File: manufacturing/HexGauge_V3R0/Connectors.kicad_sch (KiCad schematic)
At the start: 17 parts, among them J1 USB_B_Micro, J2 Conn_ARM_SWD_TC2030-NL, J3 Micro_SD_Card, J4 Conn_01x04_Pin, SW2 SW_Omron_B3FS, U4 USBLC6-4

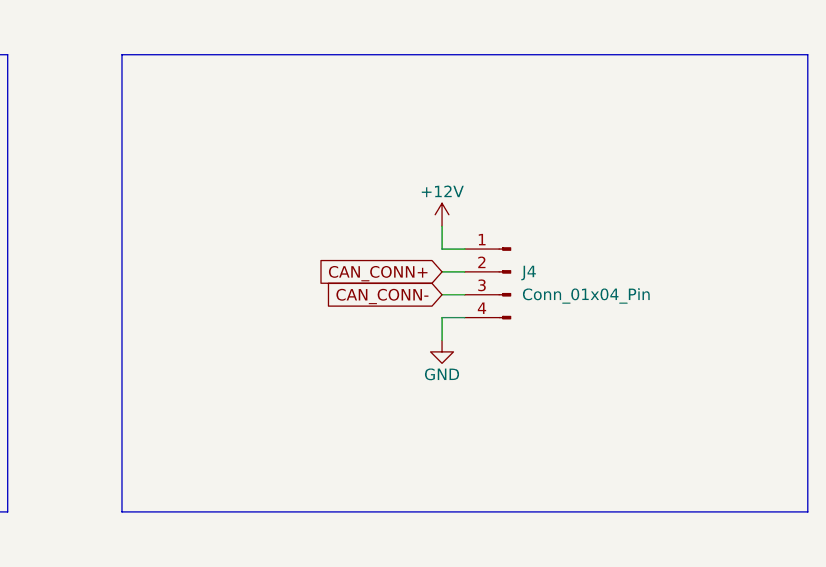
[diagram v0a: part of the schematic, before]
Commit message: Updated Board
Added Mounting Hole and 3D Packages
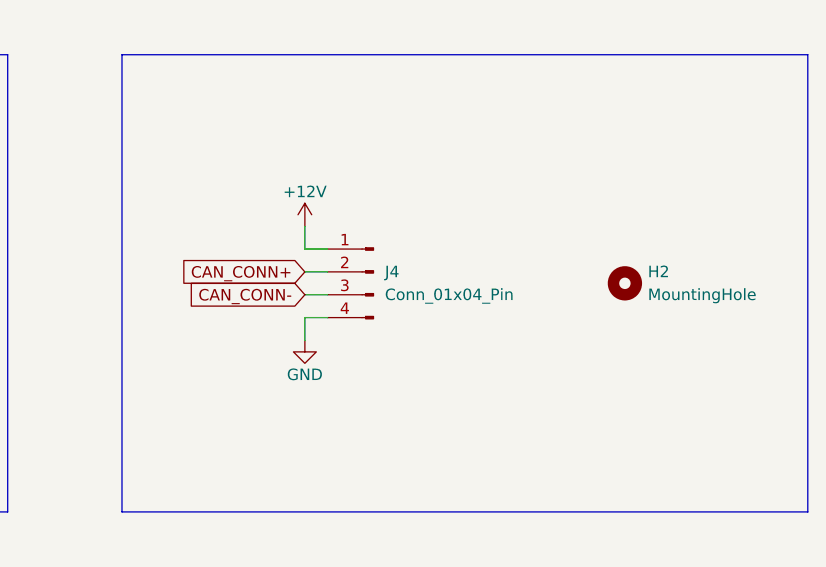
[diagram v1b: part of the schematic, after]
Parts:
- added H2: MountingHole, MountingHole:MountingHole_3.2mm_M3_Pad_Via, symbol Mechanical:MountingHole
- J1: LCSC Part # C319160 -> C397452
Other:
- moved on the sheet: J4
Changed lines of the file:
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@@
     (stroke (width 0) (type default))
   )
-  (wire (pts (xy 226.06 128.27) (xy 228.6 128.27))
+  (wire (pts (xy 210.82 128.27) (xy 213.36 128.27))
     (stroke (width 0) (type default))
   )
@@
     (stroke (width 0) (type default))
   )
-  (wire (pts (xy 226.06 125.73) (xy 228.6 125.73))
+  (wire (pts (xy 210.82 125.73) (xy 213.36 125.73))
     (stroke (width 0) (type default))
   )
@@
     (stroke (width 0) (type default))
   )
-  (wire (pts (xy 226.06 120.65) (xy 226.06 123.19))
+  (wire (pts (xy 210.82 120.65) (xy 210.82 123.19))
     (stroke (width 0) (type default))
   )
@@
     (stroke (width 0) (type default))
   )
-  (wire (pts (xy 226.06 123.19) (xy 228.6 123.19))
+  (wire (pts (xy 210.82 123.19) (xy 213.36 123.19))
     (stroke (width 0) (type default))
   )
@@
     (stroke (width 0) (type default))
   )
-  (wire (pts (xy 226.06 130.81) (xy 228.6 130.81))
+  (wire (pts (xy 210.82 130.81) (xy 213.36 130.81))
     (stroke (width 0) (type default))
   )
@@
     (stroke (width 0) (type default))
   )
-  (wire (pts (xy 226.06 130.81) (xy 226.06 133.35))
+  (wire (pts (xy 210.82 130.81) (xy 210.82 133.35))
     (stroke (width 0) (type default))
   )
@@
     )
   )
-  (global_label "CAN_CONN+" (shape input) (at 226.06 125.73 180) (fields_autoplaced)
-    (effects (font (size 1.27 1.27)) (justify right))
-    (property "Intersheetrefs" "${INTERSHEET_REFS}" (at 211.6636 125.73 0)
+  (global_label "CAN_CONN+" (shape input) (at 210.82 125.73 180) (fields_autoplaced)
+    (effects (font (size 1.27 1.27)) (justify right))
+    (property "Intersheetrefs" "${INTERSHEET_REFS}" (at 196.4236 125.73 0)
       (effects (font (size 1.27 1.27)) (justify right) hide)
     )
@@
     )
   )
-  (global_label "CAN_CONN-" (shape input) (at 226.06 128.27 180) (fields_autoplaced)
-    (effects (font (size 1.27 1.27)) (justify right))
-    (property "Intersheetrefs" "${INTERSHEET_REFS}" (at 211.6636 128.27 0)
+  (global_label "CAN_CONN-" (shape input) (at 210.82 128.27 180) (fields_autoplaced)
+    (effects (font (size 1.27 1.27)) (justify right))
+    (property "Intersheetrefs" "${INTERSHEET_REFS}" (at 196.4236 128.27 0)
       (effects (font (size 1.27 1.27)) (justify right) hide)
     )
@@
     )
   )
-  (symbol (lib_id "power:+12V") (at 226.06 120.65 0) (unit 1)
-    (in_bom yes) (on_board yes) (dnp no)
-    (property "Reference" "#PWR056" (at 226.06 124.46 0)
-      (effects (font (size 1.27 1.27)) hide)
-    )
-    (property "Value" "+12V" (at 226.06 116.84 0)
-      (effects (font (size 1.27 1.27)))
-    )
-    (property "Footprint" "" (at 226.06 120.65 0)
-      (effects (font (size 1.27 1.27)) hide)
-    )
-    (property "Datasheet" "" (at 226.06 120.65 0)
+  (symbol (lib_id "power:+12V") (at 210.82 120.65 0) (unit 1)
+    (in_bom yes) (on_board yes) (dnp no)
+    (property "Reference" "#PWR056" (at 210.82 124.46 0)
+      (effects (font (size 1.27 1.27)) hide)
+    )
+    (property "Value" "+12V" (at 210.82 116.84 0)
+      (effects (font (size 1.27 1.27)))
+    )
+    (property "Footprint" "" (at 210.82 120.65 0)
+      (effects (font (size 1.27 1.27)) hide)
+    )
+    (property "Datasheet" "" (at 210.82 120.65 0)
       (effects (font (size 1.27 1.27)) hide)
     )
@@
       (effects (font (size 1.27 1.27)) hide)
     )
-    (property "LCSC Part #" "C319160" (at 81.28 58.42 0)
+    (property "LCSC Part #" "C397452" (at 81.28 58.42 0)
       (effects (font (size 1.27 1.27)) hide)
     )
@@
     )
   )
+  (symbol (lib_id "Mechanical:MountingHole") (at 246.38 127 0) (unit 1)
+    (in_bom yes) (on_board yes) (dnp no) (fields_autoplaced)
+    (property "Reference" "H2" (at 248.92 125.73 0)
+      (effects (font (size 1.27 1.27)) (justify left))
+    )
+    (property "Value" "MountingHole" (at 248.92 128.27 0)
+      (effects (font (size 1.27 1.27)) (justify left))
+    )
+    (property "Footprint" "MountingHole:MountingHole_3.2mm_M3_Pad_Via" (at 246.38 127 0)
+      (effects (font (size 1.27 1.27)) hide)
+    )
+    (property "Datasheet" "~" (at 246.38 127 0)
+      (effects (font (size 1.27 1.27)) hide)
+    )
+    (instances
+      (project "STM32F4_HexGauge_V3"
+        (path "/1671c3d2-535f-4cd5-a65b-02e5c9ad18e5/6132b015-8d81-4c9d-ab7f-afd3c7f45a00"
+          (reference "H2") (unit 1)
+        )
+      )
+    )
+  )
   (symbol (lib_id "power:GND") (at 152.4 76.2 0) (unit 1)
     (in_bom yes) (on_board yes) (dnp no)
@@
     )
   )
-  (symbol (lib_id "Connector:Conn_01x04_Pin") (at 233.68 125.73 0) (mirror y) (unit 1)
+  (symbol (lib_id "Connector:Conn_01x04_Pin") (at 218.44 125.73 0) (mirror y) (unit 1)
     (in_bom yes) (on_board yes) (dnp no) (fields_autoplaced)
-    (property "Reference" "J4" (at 234.95 125.73 0)
+    (property "Reference" "J4" (at 219.71 125.73 0)
       (effects (font (size 1.27 1.27)) (justify right))
     )
-    (property "Value" "Conn_01x04_Pin" (at 234.95 128.27 0)
+    (property "Value" "Conn_01x04_Pin" (at 219.71 128.27 0)
       (effects (font (size 1.27 1.27)) (justify right))
     )
-    (property "Footprint" "Connector_Molex:Molex_Micro-Latch_53253-0470_1x04_P2.00mm_Vertical" (at 233.68 125.73 0)
-      (effects (font (size 1.27 1.27)) hide)
-    )
-    (property "Datasheet" "~" (at 233.68 125.73 0)
+    (property "Footprint" "Connector_Molex:Molex_Micro-Latch_53253-0470_1x04_P2.00mm_Vertical" (at 218.44 125.73 0)
+      (effects (font (size 1.27 1.27)) hide)
+    )
+    (property "Datasheet" "~" (at 218.44 125.73 0)
       (effects (font (size 1.27 1.27)) hide)
     )
@@
     )
   )
-  (symbol (lib_id "power:GND") (at 226.06 133.35 0) (unit 1)
-    (in_bom yes) (on_board yes) (dnp no)
-    (property "Reference" "#PWR057" (at 226.06 139.7 0)
-      (effects (font (size 1.27 1.27)) hide)
-    )
-    (property "Value" "GND" (at 226.06 137.16 0)
-      (effects (font (size 1.27 1.27)))
-    )
-    (property "Footprint" "" (at 226.06 133.35 0)
-      (effects (font (size 1.27 1.27)) hide)
-    )
-    (property "Datasheet" "" (at 226.06 133.35 0)
-      (effects (font (size 1.27 1.27)) hide)
-    )
+  (symbol (lib_id "power:GND") (at 210.82 133.35 0) (unit 1)
+    (in_bom yes) (on_board yes) (dnp no)
+    (property "Reference" "#PWR057" (at 210.82 139.7 0)
+      (effects (font (size 1.27 1.27)) hide)
+    )
+    (property "Value" "GND" (at 210.82 137.16 0)
+      (effects (font (size 1.27 1.27)))
+    )
+    (property "Footprint" "" (at 210.82 133.35 0)
+      (effects (font (size 1.27 1.27)) hide)
+    )
+    (property "Datasheet" "" (at 210.82 133.35 0)
+      (effects (font (size 1.27 1.27)) hide)
+    )

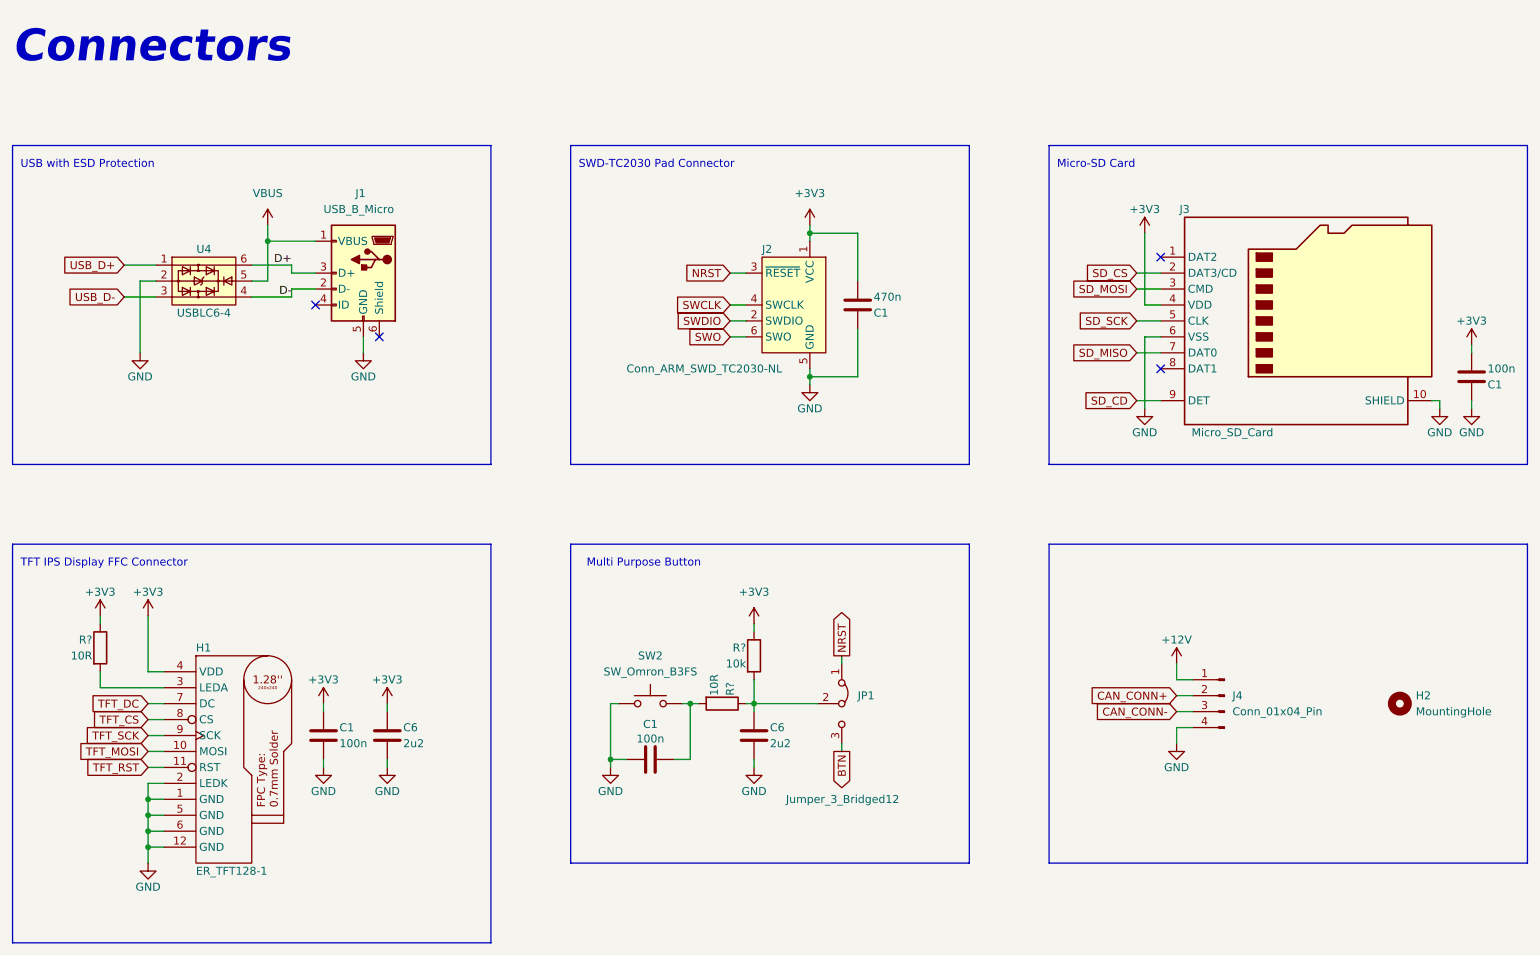
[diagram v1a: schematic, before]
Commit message: Updated Board and added Images
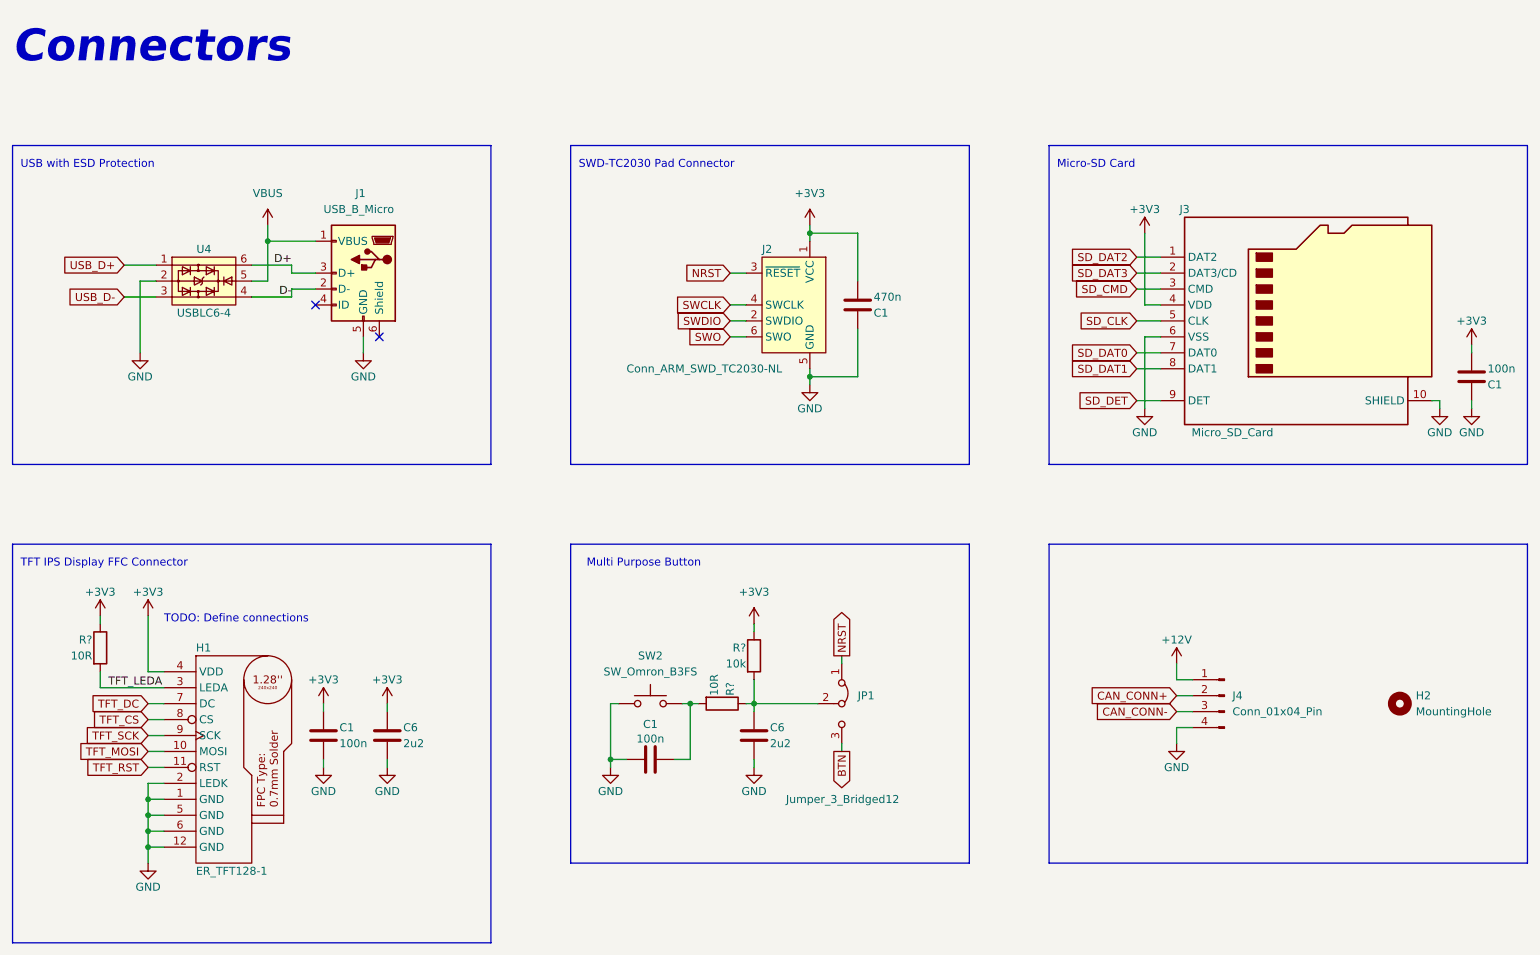
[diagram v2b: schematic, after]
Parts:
- C1: footprint Capacitor_SMD:C_0402_1005Metric -> Capacitor_SMD:C_0805_2012Metric_Pad1.18x1.45mm_HandSolder; LCSC Part # C1525 -> (none)
- C6: footprint Capacitor_SMD:C_0603_1608Metric -> Capacitor_SMD:C_0805_2012Metric_Pad1.18x1.45mm_HandSolder; LCSC Part # C23630 -> (none)
- R?: footprint Resistor_SMD:R_0402_1005Metric -> Resistor_SMD:R_0805_2012Metric_Pad1.20x1.40mm_HandSolder; LCSC Part # C25077 -> (none)
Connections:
- net TFT_LEDA: now reaches H1.3 (LEDA), R?.2
- net SD_DAT2: now reaches J3.1 (DAT2)
- net SD_DAT1: now reaches J3.8 (DAT1)
- net SD_CD renamed SD_DET
- net SD_CS renamed SD_DAT3
- net SD_MISO renamed SD_DAT0
- net SD_MOSI renamed SD_CMD
- net SD_SCK renamed SD_CLK
- no-connect marks 4 -> 2
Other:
- note added: "TODO: Define connections"
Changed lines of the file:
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@@
   (junction (at 120.65 135.89) (diameter 0) (color 0 0 0 0)
   )
-  (no_connect (at 208.28 73.66))
   (no_connect (at 73.66 63.5))
   (no_connect (at 83.82 68.58))
-  (no_connect (at 208.28 55.88))
   (wire (pts (xy 46.99 139.7) (xy 46.99 142.24))
     (stroke (width 0) (type default))
@@
     (stroke (width 0) (type default))
   )
+  (wire (pts (xy 204.47 55.88) (xy 208.28 55.88))
+    (stroke (width 0) (type default))
+  )
   (wire (pts (xy 210.82 120.65) (xy 210.82 123.19))
     (stroke (width 0) (type default))
@@
   )
   (wire (pts (xy 139.7 68.58) (xy 142.24 68.58))
+    (stroke (width 0) (type default))
+  )
+  (wire (pts (xy 204.47 73.66) (xy 208.28 73.66))
     (stroke (width 0) (type default))
   )
@@
     (effects (font (size 1.27 1.27)) (justify left bottom))
   )
+  (text "TODO: Define connections" (at 49.53 114.3 0)
+    (effects (font (size 1.27 1.27)) (justify left bottom))
+  )
   (text "Connectors" (at 25.4 25.4 0)
     (effects (font (size 5.08 5.08) (thickness 1.016) bold italic) (justify left bottom))
@@
     (effects (font (size 1.27 1.27)) (justify left bottom))
   )
+  (label "TFT_LEDA" (at 40.64 124.46 0) (fields_autoplaced)
+    (effects (font (size 1.27 1.27)) (justify left bottom))
+  )
   (label "D+" (at 69.85 57.15 180) (fields_autoplaced)
     (effects (font (size 1.27 1.27)) (justify right bottom))
@@
     )
   )
-  (global_label "SD_CD" (shape input) (at 204.47 78.74 180) (fields_autoplaced)
-    (effects (font (size 1.27 1.27)) (justify right))
-    (property "Intersheetrefs" "${INTERSHEET_REFS}" (at 195.5771 78.74 0)
-      (effects (font (size 1.27 1.27)) (justify right) hide)
-    )
-  )
-  (global_label "SD_CS" (shape input) (at 204.47 58.42 180) (fields_autoplaced)
-    (effects (font (size 1.27 1.27)) (justify right))
-    (property "Intersheetrefs" "${INTERSHEET_REFS}" (at 195.6376 58.42 0)
+  (global_label "SD_DET" (shape input) (at 204.47 78.74 180) (fields_autoplaced)
+    (effects (font (size 1.27 1.27)) (justify right))
+    (property "Intersheetrefs" "${INTERSHEET_REFS}" (at 194.7305 78.74 0)
+      (effects (font (size 1.27 1.27)) (justify right) hide)
+    )
+  )
+  (global_label "SD_DAT2" (shape input) (at 204.47 55.88 180) (fields_autoplaced)
+    (effects (font (size 1.27 1.27)) (justify right))
+    (property "Intersheetrefs" "${INTERSHEET_REFS}" (at 193.5814 55.88 0)
+      (effects (font (size 1.27 1.27)) (justify right) hide)
+    )
+  )
+  (global_label "SD_DAT3" (shape input) (at 204.47 58.42 180) (fields_autoplaced)
+    (effects (font (size 1.27 1.27)) (justify right))
+    (property "Intersheetrefs" "${INTERSHEET_REFS}" (at 193.5814 58.42 0)
       (effects (font (size 1.27 1.27)) (justify right) hide)
     )
@@
     )
   )
-  (global_label "SD_MOSI" (shape input) (at 204.47 60.96 180) (fields_autoplaced)
-    (effects (font (size 1.27 1.27)) (justify right))
-    (property "Intersheetrefs" "${INTERSHEET_REFS}" (at 193.5209 60.96 0)
+  (global_label "SD_CMD" (shape input) (at 204.47 60.96 180) (fields_autoplaced)
+    (effects (font (size 1.27 1.27)) (justify right))
+    (property "Intersheetrefs" "${INTERSHEET_REFS}" (at 194.1257 60.96 0)
       (effects (font (size 1.27 1.27)) (justify right) hide)
     )
@@
     )
   )
-  (global_label "SD_MISO" (shape input) (at 204.47 71.12 180) (fields_autoplaced)
-    (effects (font (size 1.27 1.27)) (justify right))
-    (property "Intersheetrefs" "${INTERSHEET_REFS}" (at 193.5209 71.12 0)
-      (effects (font (size 1.27 1.27)) (justify right) hide)
-    )
-  )
-  (global_label "SD_SCK" (shape input) (at 204.47 66.04 180) (fields_autoplaced)
-    (effects (font (size 1.27 1.27)) (justify right))
-    (property "Intersheetrefs" "${INTERSHEET_REFS}" (at 194.3676 66.04 0)
+  (global_label "SD_DAT0" (shape input) (at 204.47 71.12 180) (fields_autoplaced)
+    (effects (font (size 1.27 1.27)) (justify right))
+    (property "Intersheetrefs" "${INTERSHEET_REFS}" (at 193.5814 71.12 0)
+      (effects (font (size 1.27 1.27)) (justify right) hide)
+    )
+  )
+  (global_label "SD_CLK" (shape input) (at 204.47 66.04 180) (fields_autoplaced)
+    (effects (font (size 1.27 1.27)) (justify right))
+    (property "Intersheetrefs" "${INTERSHEET_REFS}" (at 194.549 66.04 0)
+      (effects (font (size 1.27 1.27)) (justify right) hide)
+    )
+  )
+  (global_label "SD_DAT1" (shape input) (at 204.47 73.66 180) (fields_autoplaced)
+    (effects (font (size 1.27 1.27)) (justify right))
+    (property "Intersheetrefs" "${INTERSHEET_REFS}" (at 193.5814 73.66 0)
       (effects (font (size 1.27 1.27)) (justify right) hide)
     )
@@
       (effects (font (size 1.27 1.27)) (justify left))
     )
-    (property "Footprint" "Capacitor_SMD:C_0402_1005Metric" (at 258.7752 78.74 0)
+    (property "Footprint" "Capacitor_SMD:C_0805_2012Metric_Pad1.18x1.45mm_HandSolder" (at 258.7752 78.74 0)
       (effects (font (size 1.27 1.27)) hide)
     )
@@
       (effects (font (size 1.27 1.27)) hide)
     )
-    (property "LCSC Part #" "C1525" (at 257.81 74.93 0)
+    (property "LCSC Part #" "" (at 257.81 74.93 0)
       (effects (font (size 1.27 1.27)) hide)
     )
@@
       (effects (font (size 1.27 1.27)) (justify left))
     )
-    (property "Footprint" "Capacitor_SMD:C_0603_1608Metric" (at 86.0552 135.89 0)
+    (property "Footprint" "Capacitor_SMD:C_0805_2012Metric_Pad1.18x1.45mm_HandSolder" (at 86.0552 135.89 0)
       (effects (font (size 1.27 1.27)) hide)
     )
@@
       (effects (font (size 1.27 1.27)) hide)
     )
-    (property "LCSC Part #" "C23630" (at 85.09 132.08 0)
+    (property "LCSC Part #" "" (at 85.09 132.08 0)
       (effects (font (size 1.27 1.27)) hide)
     )
@@
       (effects (font (size 1.27 1.27)) (justify right))
     )
-    (property "Footprint" "Resistor_SMD:R_0402_1005Metric" (at 37.592 118.11 90)
+    (property "Footprint" "Resistor_SMD:R_0805_2012Metric_Pad1.20x1.40mm_HandSolder" (at 37.592 118.11 90)
       (effects (font (size 1.27 1.27)) hide)
     )
@@
       (effects (font (size 1.27 1.27)) hide)
     )
-    (property "LCSC Part #" "C25077" (at 39.37 118.11 0)
+    (property "LCSC Part #" "" (at 39.37 118.11 0)
       (effects (font (size 1.27 1.27)) hide)
     )
@@
       (effects (font (size 1.27 1.27)) (justify left))
     )
-    (property "Footprint" "Capacitor_SMD:C_0402_1005Metric" (at 75.8952 135.89 0)
+    (property "Footprint" "Capacitor_SMD:C_0805_2012Metric_Pad1.18x1.45mm_HandSolder" (at 75.8952 135.89 0)
       (effects (font (size 1.27 1.27)) hide)
     )
@@
       (effects (font (size 1.27 1.27)) hide)
     )
-    (property "LCSC Part #" "C1525" (at 74.93 132.08 0)
+    (property "LCSC Part #" "" (at 74.93 132.08 0)
       (effects (font (size 1.27 1.27)) hide)
     )
@@
       (effects (font (size 1.27 1.27)) hide)
     )
-    (property "Datasheet" "https://datasheet.lcsc.com/lcsc/2110151630_XKB-Connectivity-XKTF-015-N_C381082.pdf" (at 231.14 63.5 0)
-      (effects (font (size 1.27 1.27)) hide)
-    )
+    (property "Datasheet" "https://datasheet.lcsc.com/lcsc/1912111437_MOLEX-5033981892_C428492.pdf" (at 231.14 63.5 0)
+      (effects (font (size 1.27 1.27)) hide)
+    )
